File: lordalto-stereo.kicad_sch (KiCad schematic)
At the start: 1 part

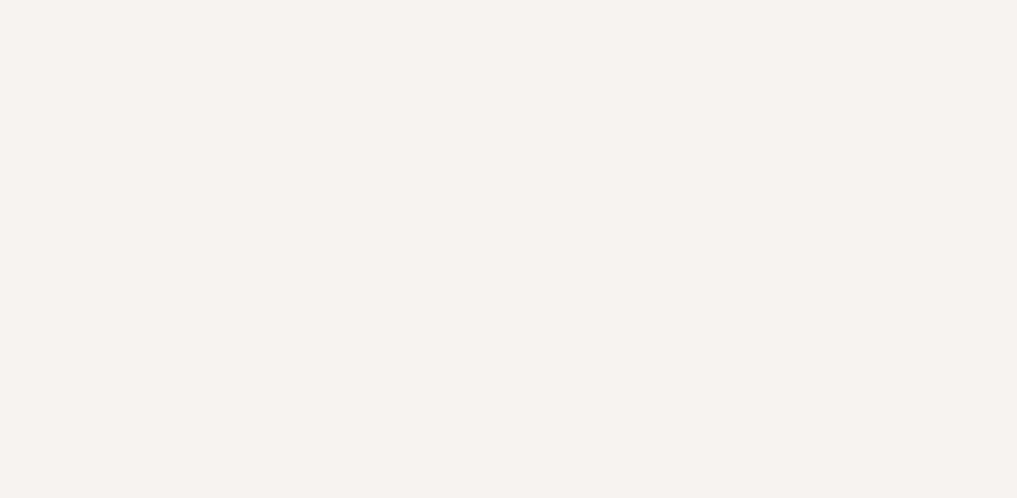
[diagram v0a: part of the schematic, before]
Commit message: Added Power Stage and Started Work on Buck
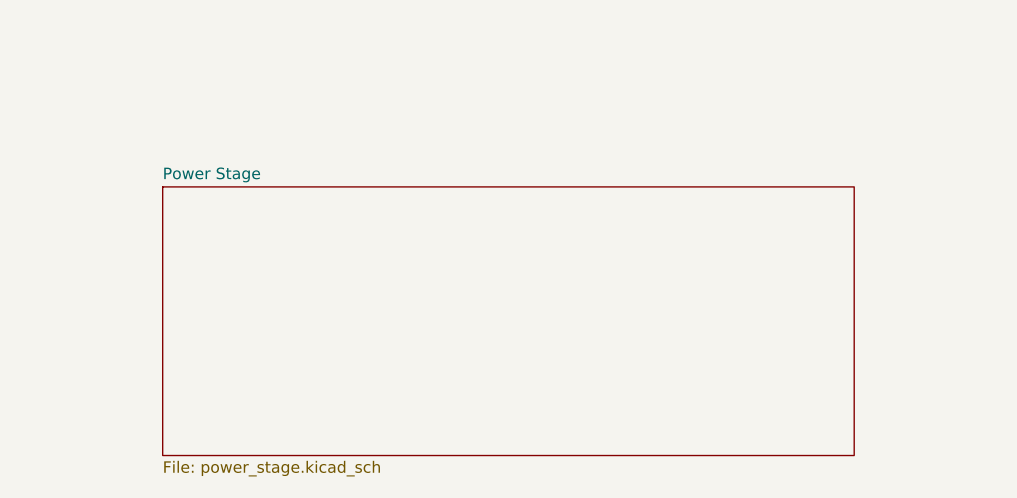
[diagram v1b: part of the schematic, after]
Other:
- added sheet Power Stage (power_stage.kicad_sch)
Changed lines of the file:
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@@
+	)
+	(sheet
+		(at 69.85 156.845)
+		(size 76.835 29.845)
+		(exclude_from_sim no)
+		(in_bom yes)
+		(on_board yes)
+		(dnp no)
+		(fields_autoplaced yes)
+		(stroke
+			(width 0.1524)
+			(type solid)
+		)
+		(fill
+			(color 0 0 0 0)
+		)
+		(property "Sheetname" "Power Stage"
+			(at 69.85 156.1334 0)
+			(show_name no)
+			(do_not_autoplace no)
+			(effects
+				(font
+					(size 1.27 1.27)
+				)
+				(justify left bottom)
+			)
+		)
+		(property "Sheetfile" "power_stage.kicad_sch"
+			(at 69.85 187.2746 0)
+			(show_name no)
+			(do_not_autoplace no)
+			(effects
+				(font
+					(size 1.27 1.27)
+				)
+				(justify left top)
+			)
+		)
+		(instances
+			(project "lordalto-stereo"
+				(path "/2a301b58-646d-43ef-90e5-21c6e30fbc64"
+					(page "4")
+				)
+			)
+		)
 	)
 	(sheet
